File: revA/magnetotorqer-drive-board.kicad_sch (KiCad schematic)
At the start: 38 parts, among them J1 ZX62-AB-5PA(31), J2 T1M-02-F-SH-L, J3 T1M-02-F-SH-L, J4 T1M-02-F-SH-L, J5 T1M-02-F-SH-L, J6 T1M-02-F-SH-L, J7 T1M-02-F-SH-L, P1 Card Edge for HSEC8-160-01-S-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, U1 74LVC1G17, U2 74LVC1G17, U3 MCP9700AT-E/LT, U4 MCP9700AT-E/LT

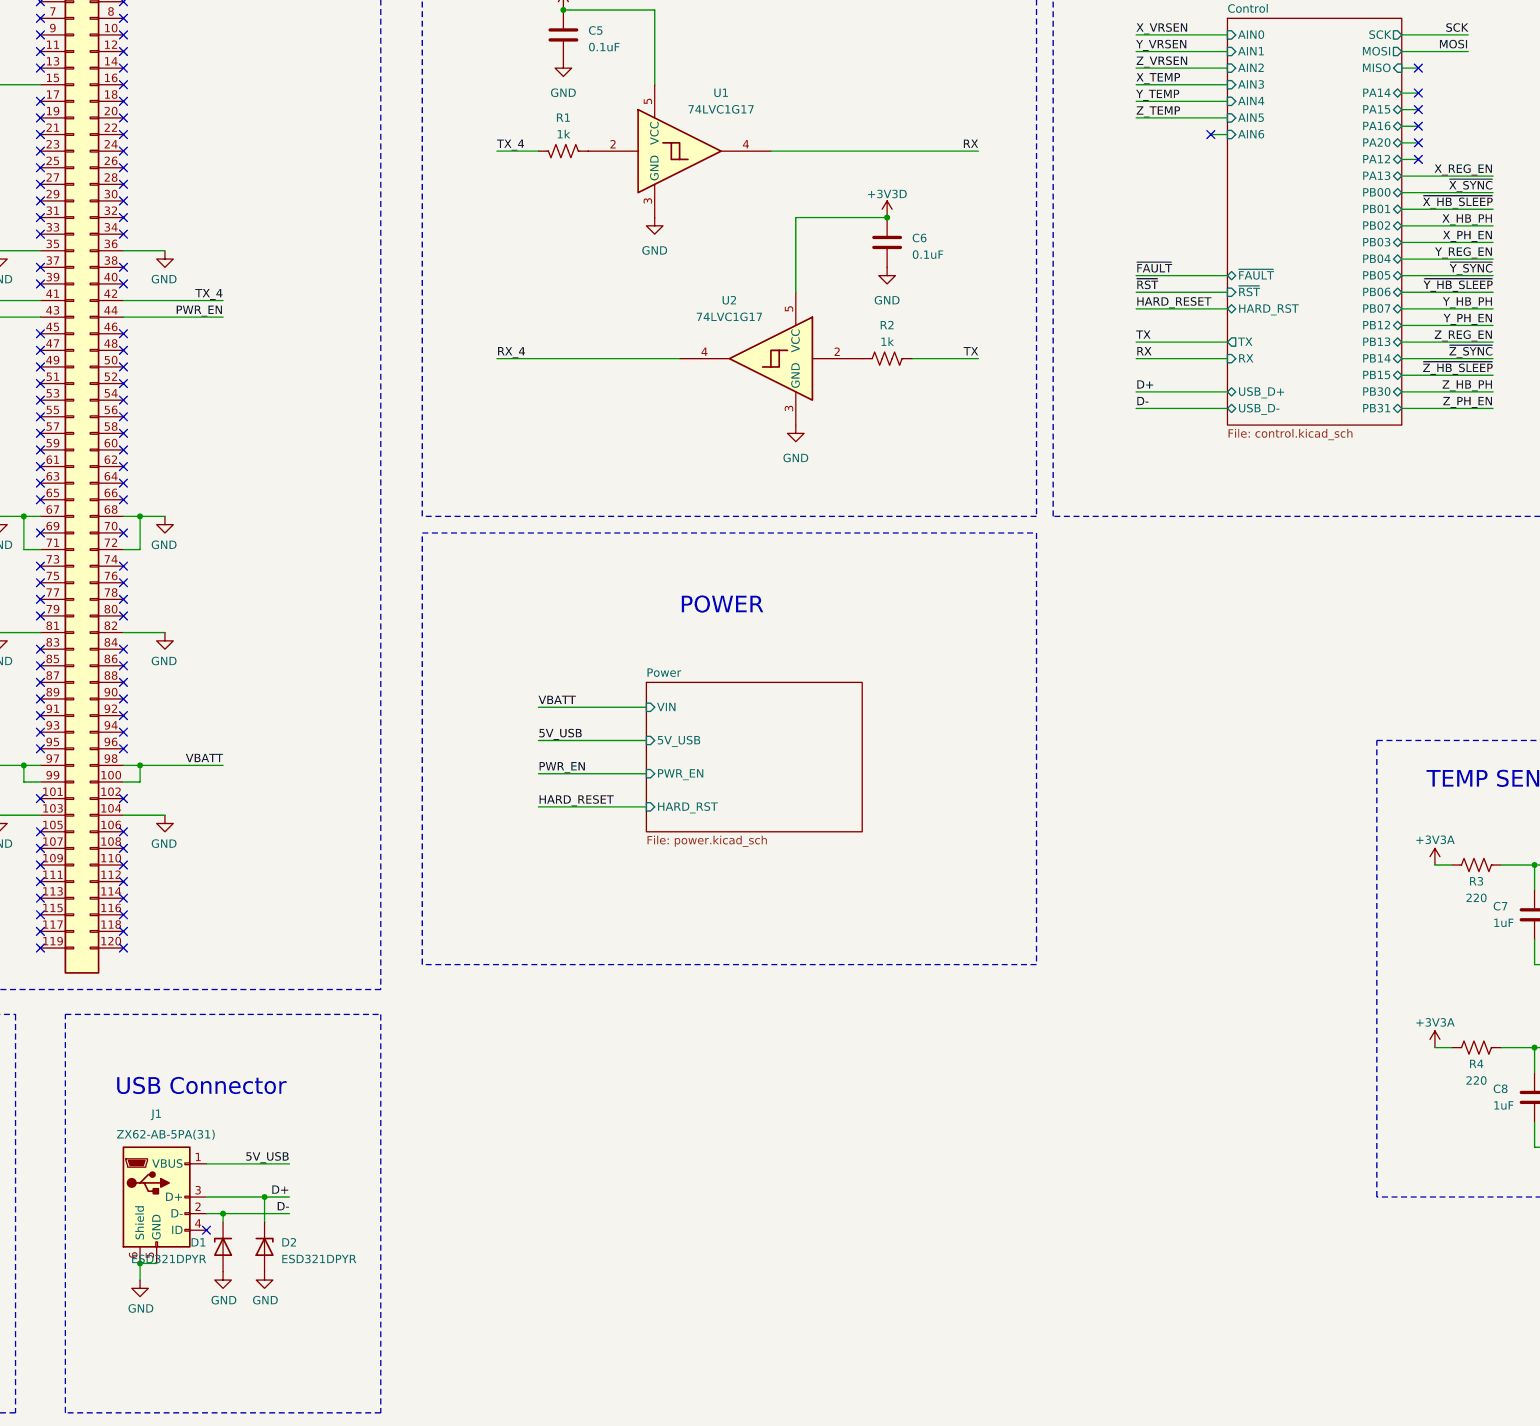
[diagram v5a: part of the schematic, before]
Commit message: routing mostly complete
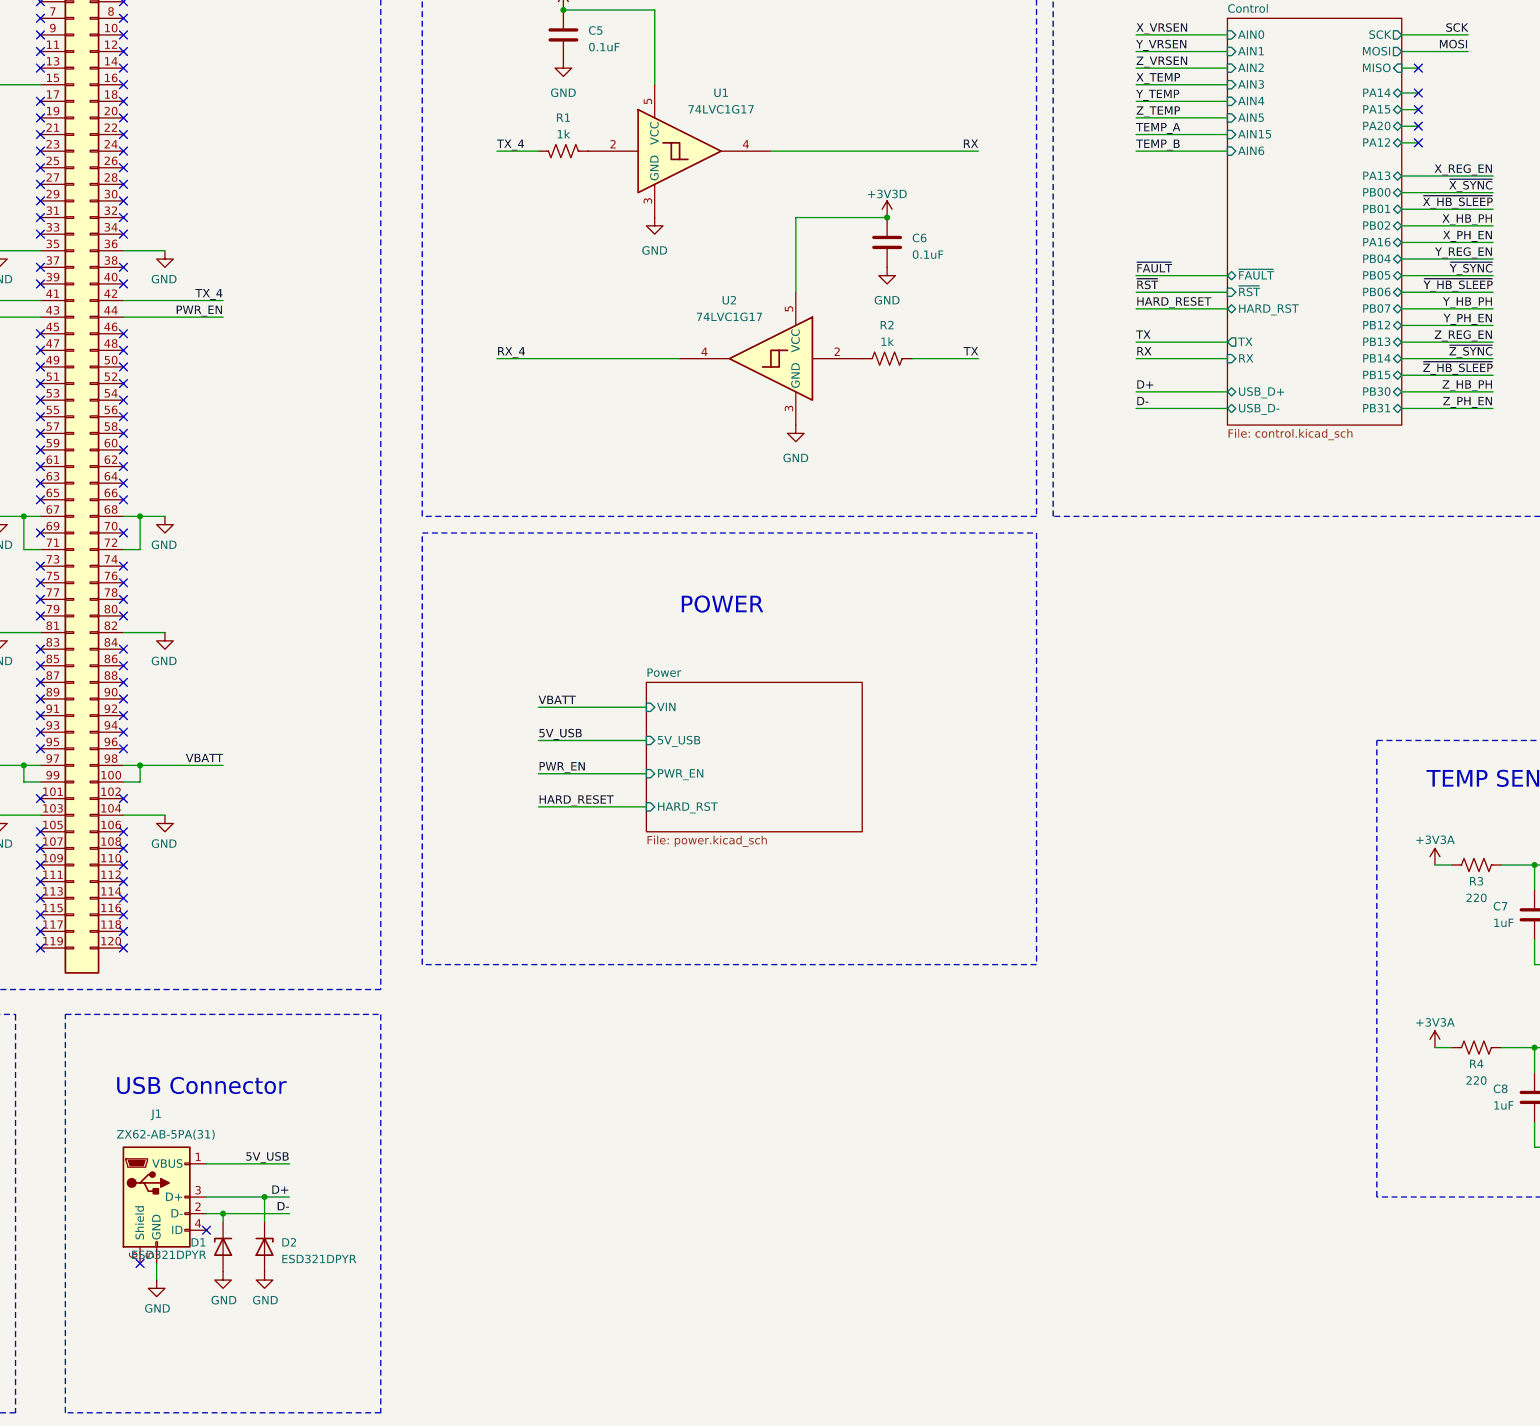
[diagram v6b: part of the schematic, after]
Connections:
- net GND: no longer J1.6 (Shield)
- no-connect marks 109 -> 108
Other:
- sheet Control ports: added AIN15; removed PB03
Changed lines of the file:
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@@
 (kicad_sch (version 20230121) (generator eeschema)
   (paper "B")
-  (junction (at 71.12 226.06) (diameter 0) (color 0 0 0 0)
-  )
   (junction (at 284.48 193.04) (diameter 0) (color 0 0 0 0)
   )
@@
   (no_connect (at 68.58 124.46))
   (no_connect (at 68.58 68.58))
-  (no_connect (at 266.7 52.07))
   (no_connect (at 55.88 66.04))
   (no_connect (at 68.58 121.92))
@@
   (no_connect (at 55.88 144.78))
   (no_connect (at 68.58 53.34))
-  (no_connect (at 266.7 57.15))
+  (no_connect (at 266.7 54.61))
   (no_connect (at 55.88 127))
   (no_connect (at 68.58 73.66))
@@
   (no_connect (at 55.88 99.06))
   (no_connect (at 68.58 38.1))
+  (no_connect (at 71.12 226.06))
   (no_connect (at 55.88 137.16))
   (no_connect (at 68.58 172.72))
@@
   (no_connect (at 55.88 134.62))
   (no_connect (at 266.7 46.99))
-  (no_connect (at 234.95 53.34))
   (no_connect (at 55.88 91.44))
   (no_connect (at 55.88 124.46))
-  (no_connect (at 266.7 54.61))
+  (no_connect (at 266.7 52.07))
   (no_connect (at 68.58 96.52))
   (no_connect (at 55.88 63.5))
@@
     (stroke (width 0) (type default))
   )
-  (wire (pts (xy 71.12 226.06) (xy 71.12 228.6))
-    (stroke (width 0) (type default))
-  )
   (wire (pts (xy 83.82 218.44) (xy 93.98 218.44))
     (stroke (width 0) (type default))
@@
     (stroke (width 0) (type default))
   )
+  (wire (pts (xy 73.66 226.06) (xy 73.66 228.6))
+    (stroke (width 0) (type default))
+  )
   (wire (pts (xy 279.4 165.1) (xy 284.48 165.1))
     (stroke (width 0) (type default))
@@
     (stroke (width 0) (type default))
   )
-  (wire (pts (xy 71.12 226.06) (xy 73.66 226.06))
-    (stroke (width 0) (type default))
-  )
   (wire (pts (xy 284.48 208.28) (xy 284.48 204.47))
     (stroke (width 0) (type default))
@@
     (stroke (width 0) (type default))
   )
-  (wire (pts (xy 234.95 53.34) (xy 237.49 53.34))
+  (wire (pts (xy 223.52 55.88) (xy 237.49 55.88))
     (stroke (width 0) (type default))
   )
@@
     (stroke (width 0) (type default))
   )
+  (wire (pts (xy 223.52 53.34) (xy 237.49 53.34))
+    (stroke (width 0) (type default))
+  )
   (wire (pts (xy 264.16 80.01) (xy 278.13 80.01))
     (stroke (width 0) (type default))
@@
     (stroke (width 0) (type default))
   )
-  (wire (pts (xy 264.16 54.61) (xy 266.7 54.61))
+  (wire (pts (xy 264.16 52.07) (xy 266.7 52.07))
     (stroke (width 0) (type default))
   )
@@
     (stroke (width 0) (type default))
   )
-  (wire (pts (xy 264.16 57.15) (xy 266.7 57.15))
+  (wire (pts (xy 264.16 54.61) (xy 266.7 54.61))
     (stroke (width 0) (type default))
   )
@@
     (stroke (width 0) (type default))
   )
-  (wire (pts (xy 264.16 52.07) (xy 266.7 52.07))
-    (stroke (width 0) (type default))
-  )
   (rectangle (start 16.51 16.51) (end 107.95 184.15)
     (stroke (width 0) (type dash))
@@
     (effects (font (size 1.27 1.27)) (justify right bottom))
   )
+  (label "TEMP_A" (at 223.52 53.34 0) (fields_autoplaced)
+    (effects (font (size 1.27 1.27)) (justify left bottom))
+  )
   (label "Y_TEMP" (at 383.54 182.88 180) (fields_autoplaced)
     (effects (font (size 1.27 1.27)) (justify right bottom))
@@
     (effects (font (size 1.27 1.27)) (justify left bottom))
   )
+  (label "TEMP_B" (at 223.52 55.88 0) (fields_autoplaced)
+    (effects (font (size 1.27 1.27)) (justify left bottom))
+  )
   (label "Y_TEMP" (at 223.52 48.26 0) (fields_autoplaced)
     (effects (font (size 1.27 1.27)) (justify left bottom))
@@
     )
   )
+  (symbol (lib_id "power:GND") (at 73.66 228.6 0) (unit 1)
+    (in_bom yes) (on_board yes) (dnp no)
+    (property "Reference" "#PWR06" (at 73.66 234.95 0)
+      (effects (font (size 1.27 1.27)) hide)
+    )
+    (property "Value" "GND" (at 73.787 232.9942 0)
+      (effects (font (size 1.27 1.27)))
+    )
+    (property "Footprint" "" (at 73.66 228.6 0)
+      (effects (font (size 1.27 1.27)) hide)
+    )
+    (property "Datasheet" "" (at 73.66 228.6 0)
+      (effects (font (size 1.27 1.27)) hide)
+    )
+    (pin "1")
+    (instances
+      (project "magnetotorqer-drive-board"
+        (path "/612afcad-8da9-4dff-bf3c-8828929809ff"
+          (reference "#PWR06") (unit 1)
+        )
+      )
+      (project "payload-interface-board"
+        (path "/dc2801a1-d539-4721-b31f-fe196b9f13df"
+          (reference "#PWR049") (unit 1)
+        )
+      )
+    )
+  )
   (symbol (lib_id "Device:C") (at 284.48 200.66 0) (unit 1)
     (in_bom yes) (on_board yes) (dnp no)
@@
     )
   )
-  (symbol (lib_id "power:GND") (at 71.12 228.6 0) (unit 1)
-    (in_bom yes) (on_board yes) (dnp no)
-    (property "Reference" "#PWR06" (at 71.12 234.95 0)
-      (effects (font (size 1.27 1.27)) hide)
-    )
-    (property "Value" "GND" (at 71.247 232.9942 0)
-      (effects (font (size 1.27 1.27)))
-    )
-    (property "Footprint" "" (at 71.12 228.6 0)
-      (effects (font (size 1.27 1.27)) hide)
-    )
-    (property "Datasheet" "" (at 71.12 228.6 0)
-      (effects (font (size 1.27 1.27)) hide)
-    )
-    (pin "1")
-    (instances
-      (project "magnetotorqer-drive-board"
-        (path "/612afcad-8da9-4dff-bf3c-8828929809ff"
-          (reference "#PWR06") (unit 1)
-        )
-      )
-      (project "payload-interface-board"
-        (path "/dc2801a1-d539-4721-b31f-fe196b9f13df"
-          (reference "#PWR049") (unit 1)
-        )
-      )
-    )
-  )
   (symbol (lib_id "power:GND") (at 389.89 86.36 0) (mirror y) (unit 1)
     (in_bom yes) (on_board yes) (dnp no)
@@
       (effects (font (size 1.27 1.27)) (justify left))
     )
-    (property "Value" "ESD321DPYR" (at 81.28 225.425 90)
+    (property "Value" "ESD321DPYR" (at 81.28 224.79 90)
       (effects (font (size 1.27 1.27)) (justify left))
     )
@@
       (effects (font (size 1.27 1.27)) (justify left))
     )
-    (pin "AIN6" input (at 237.49 53.34 180)
+    (pin "AIN6" input (at 237.49 55.88 180)
       (effects (font (size 1.27 1.27)) (justify left))
     )
@@
       (effects (font (size 1.27 1.27)) (justify right))
     )
-    (pin "PB03" bidirectional (at 264.16 69.85 0)
-      (effects (font (size 1.27 1.27)) (justify right))
-    )
     (pin "PB04" bidirectional (at 264.16 72.39 0)
       (effects (font (size 1.27 1.27)) (justify right))
@@
       (effects (font (size 1.27 1.27)) (justify left))
     )
-    (pin "PA12" bidirectional (at 264.16 57.15 0)
+    (pin "PA12" bidirectional (at 264.16 54.61 0)
       (effects (font (size 1.27 1.27)) (justify right))
     )
@@
       (effects (font (size 1.27 1.27)) (justify right))
     )
-    (pin "PA20" bidirectional (at 264.16 54.61 0)
+    (pin "PA20" bidirectional (at 264.16 52.07 0)
       (effects (font (size 1.27 1.27)) (justify right))
     )
-    (pin "PA16" bidirectional (at 264.16 52.07 0)
+    (pin "PA16" bidirectional (at 264.16 69.85 0)
       (effects (font (size 1.27 1.27)) (justify right))
     )
@@
       (effects (font (size 1.27 1.27)) (justify left))
     )
+    (pin "AIN15" input (at 237.49 53.34 180)
+      (effects (font (size 1.27 1.27)) (justify left))
+    )

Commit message: working
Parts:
- added J8: Conn_01x06, Connector_PinHeader_2.54mm:PinHeader_1x06_P2.54mm_Vertical_SMD_Pin1Right, symbol Connector_Generic:Conn_01x06
- added R1: 100K, Resistor_SMD:R_0603_1608Metric, symbol Device:R_US
- added TP3 (x3): ${NET_NAME(1)}, SierraLobo:Keystone_5027, symbol Connector:TestPoint
- added TP3 (x5): ${NET_NAME(1)}, SierraLobo:TestPoint_Keystone_5000-5004_Miniature, symbol Connector:TestPoint
- C10: renamed from C4; Manufacturer TDK -> (none); Mfr. Part No CGA2B3X7R1H104K050BE -> (none)
- C3: renamed from C7; Manufacturer TDK -> (none); Mfr. Part No CGA3E1X7R1V105K080AE -> (none)
- C4: renamed from C9; Manufacturer TDK -> (none); Mfr. Part No CGA2B3X7R1H104K050BE -> (none)
- C5: renamed from C8; Manufacturer TDK -> (none); Mfr. Part No CGA3E1X7R1V105K080AE -> (none)
- C6: renamed from C1; Manufacturer TDK -> (none); Mfr. Part No CGA2B3X7R1H104K050BE -> (none)
- C7: renamed from C10; Manufacturer TDK -> (none); Mfr. Part No CGA2B3X7R1H104K050BE -> (none)
- C8: renamed from C2; Manufacturer TDK -> (none); Mfr. Part No CGA2B3X7R1H104K050BE -> (none)
- C9: renamed from C3; Manufacturer TDK -> (none); Mfr. Part No CGA2B3X7R1H104K050BE -> (none)
- renumbered C5 to C1, C6 to C2, J2 to J1, J3 to J2, J4 to J3, J5 to J4, J6 to J5, J7 to J6, J1 to J7, R1 to R2, R2 to R3, R3 to R4, R4 to R8
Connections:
- net Control/PA12: now also R1.1
- net GND: now also J8.1 (Pin_1), R1.2, TP3.1, TP3.1, TP3.1
- net TEMP_A: now also TP3.1
- net TEMP_B: now also TP3.1
- net X_TEMP: now also TP3.1
- net Y_TEMP: now also TP3.1
- net Z_TEMP: now also TP3.1
- net 5V_USB renamed 5V_USB_IN
- net LED_VCC renamed BUS_LED_PWR
- new net 5V_DB: J8.3 (Pin_3)
- new net RX_DEBUG: J8.4 (Pin_4)
- new net TX_DEBUG: J8.5 (Pin_5)
- no-connect marks 108 -> 104
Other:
- sheet Control ports: added RX_DEBUG, TX_DEBUG; removed none
- sheet Power ports: added 5V_DEBUG, 5V_USB_IN, BUS_LED_PWR; removed 5V_USB
- note added: "VBATT (7.2-8.4V) main power input Feeds all subsequten domains through LDOs 5V_USB & 5V_DEBUG is diode OR'd to VAA for programming/debug power."
- title: (none) -> SCHEMATIC, CUBESAT MAGNETORQER DRIVER

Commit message: worked review changes
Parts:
- added R? (x4): 0, Resistor_SMD:R_0603_1608Metric, symbol Device:R_US
- C1: renamed from C6; Manufacturer (none) -> TDK Corporation; Mfr. Part No (none) -> CGA3E2X7R1H104K080AE; Value2 (none) -> 50V
- C10: renamed from C7; Manufacturer (none) -> TDK Corporation; Mfr. Part No (none) -> CGA3E2X7R1H104K080AE; Value2 (none) -> 50V
- C2: renamed from C8; Manufacturer (none) -> TDK Corporation; Mfr. Part No (none) -> CGA3E2X7R1H104K080AE; Value2 (none) -> 50V
- C3: renamed from C9; Manufacturer (none) -> TDK Corporation; Mfr. Part No (none) -> CGA3E2X7R1H104K080AE; Value2 (none) -> 50V
- C4: renamed from C10; Manufacturer (none) -> TDK Corporation; Mfr. Part No (none) -> CGA3E2X7R1H104K080AE; Value2 (none) -> 50V
- C5: renamed from C1; Manufacturer (none) -> TDK Corporation; Mfr. Part No (none) -> CGA3E2X7R1H104K080AE; Value2 (none) -> 50V
- C6: renamed from C2; Manufacturer (none) -> TDK Corporation; Mfr. Part No (none) -> CGA3E2X7R1H104K080AE; Value2 (none) -> 50V
- C7: renamed from C3; Manufacturer (none) -> TDK Corporation; Mfr. Part No (none) -> CGA4J3X7R1H105K125AE; Value2 (none) -> 50V
- C8: renamed from C5; Manufacturer (none) -> TDK Corporation; Mfr. Part No (none) -> CGA4J3X7R1H105K125AE; Value2 (none) -> 50V
- C9: renamed from C4; Manufacturer (none) -> TDK Corporation; Mfr. Part No (none) -> CGA3E2X7R1H104K080AE; Value2 (none) -> 50V
- D1, D2: Value2 (none) -> 6.8V
- J?: renamed from J8; Manufacturer (none) -> Samtec; Mfr. Part No (none) -> TSM-136-01-L-SV
- R10: renamed from R5; Manufacturer (none) -> Stackpole Electronics Inc; Mfr. Part No (none) -> RMCF0603FT10K0; Value2 (none) -> 100mW
- R11: renamed from R6; Manufacturer (none) -> Stackpole Electronics Inc; Mfr. Part No (none) -> RMCF0603FT10K0; Value2 (none) -> 100mW
- R12: renamed from R7; Manufacturer (none) -> Stackpole Electronics Inc; Mfr. Part No (none) -> RMCF0603FT10K0; Value2 (none) -> 100mW
- R5: renamed from R2; Manufacturer (none) -> Stackpole Electronics Inc; Mfr. Part No (none) -> RMCF0603FG1K00; Value2 (none) -> 100mW
- R6: renamed from R3; Manufacturer (none) -> Stackpole Electronics Inc; Mfr. Part No (none) -> RMCF0603FG1K00; Value2 (none) -> 100mW
- R7: renamed from R4; Manufacturer (none) -> Stackpole Electronics Inc; Mfr. Part No (none) -> RMCF0603FT220R; Value2 (none) -> 100mW
- R8: Manufacturer (none) -> Stackpole Electronics Inc; Mfr. Part No (none) -> RMCF0603FT220R; Value2 (none) -> 100mW
- R9: renamed from R1; value 100K -> 100k; Manufacturer (none) -> Stackpole Electronics Inc; Mfr. Part No (none) -> RMCF0603FT100K; Value2 (none) -> 100mW
- U3, U4: value MCP9700AT-E/LT -> MCP9700Ax-E/LT; symbol Sensor_Temperature:MCP9700Ax-ELT -> SierraLobo:MCP9700Ax-E/LT; Mfr. Part No. (none) -> MCP9700AT-E/LT
- renumbered J7 to J1, J1 to J2, J2 to J3, J3 to J4, J4 to J5, J5 to J6, J6 to J7, TP3 to TP?
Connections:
- net RX_4: now also R?.1, R?.1; no longer U2.4
- net TX_4: now also R?.1, R?.1; no longer R5.1
- new net RX_IN: R?.2, R?.2, U2.4
- new net TX_IN: R5.1, R?.2, R?.2
- no-connect marks 104 -> 106
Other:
- moved on the sheet: C5, C6, R5, R6, U1, U2
